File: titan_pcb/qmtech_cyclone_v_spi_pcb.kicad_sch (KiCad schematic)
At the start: 5 parts, among them J1 FPGA U8, J2 FPGA U7, J3 DUMMY_JTAG, U1 ESP32-DevKitC, U2 Teensy3.2

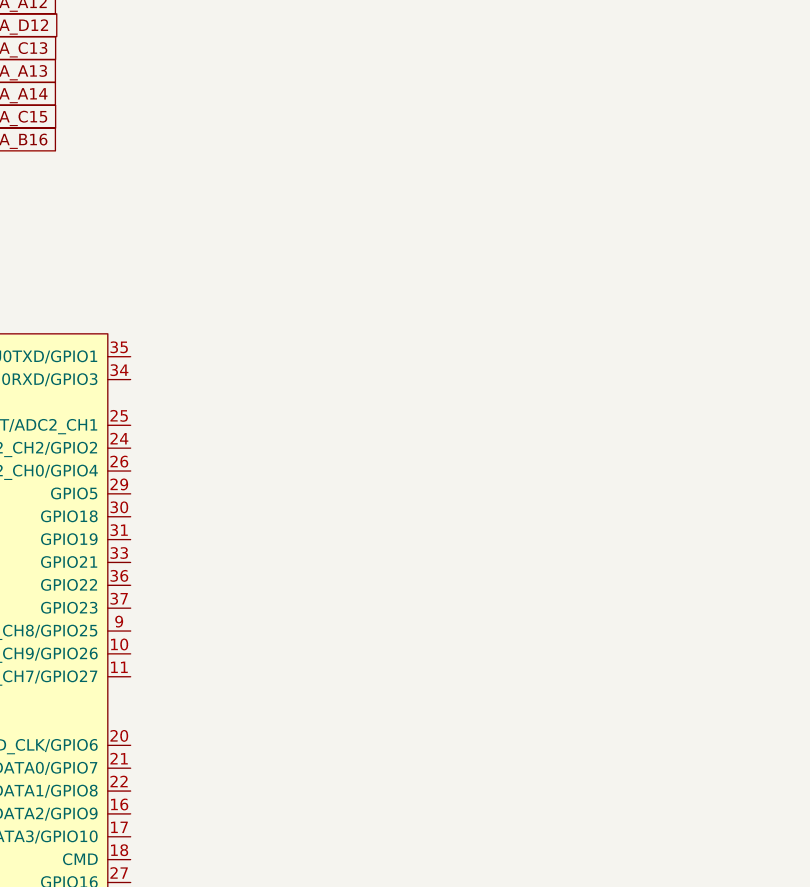
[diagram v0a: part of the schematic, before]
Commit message: added pico to pcb
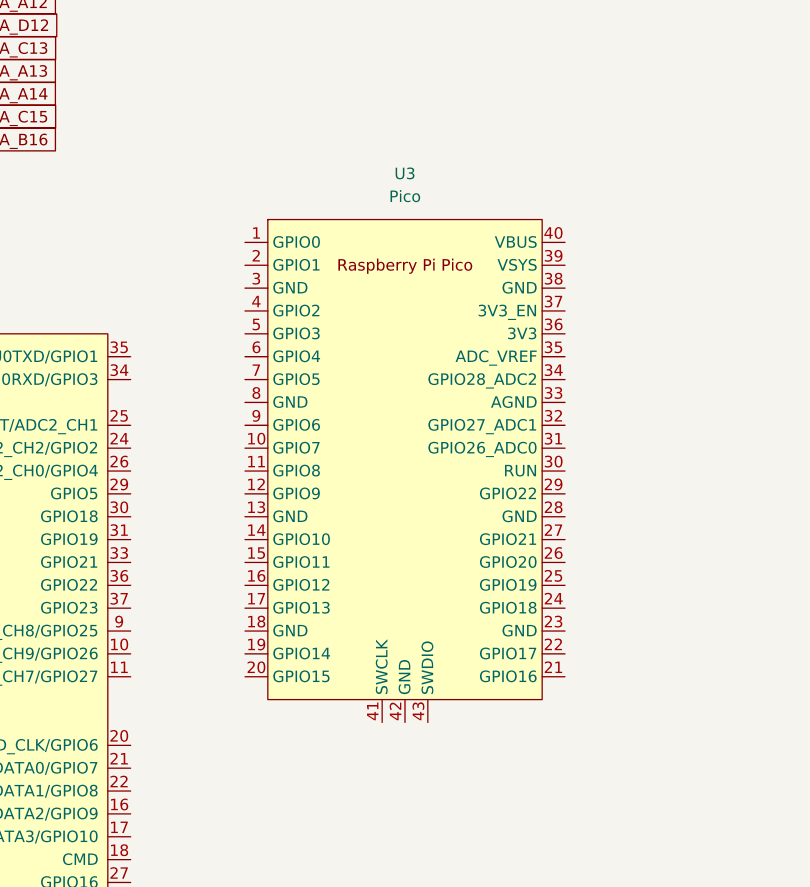
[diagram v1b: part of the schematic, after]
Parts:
- added U3: Pico, MCU_RaspberryPi_and_Boards:RPi_Pico_SMD_TH, symbol MCU_RaspberryPi_and_Boards:Pico
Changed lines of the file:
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@@
+    )
+  )
+  (symbol (lib_id "MCU_RaspberryPi_and_Boards:Pico") (at 176.53 133.35 0) (unit 1)
+    (in_bom yes) (on_board yes) (dnp no) (fields_autoplaced)
+    (property "Reference" "U3" (at 176.53 101.6 0)
+      (effects (font (size 1.27 1.27)))
+    )
+    (property "Value" "Pico" (at 176.53 104.14 0)
+      (effects (font (size 1.27 1.27)))
+    )
+    (property "Footprint" "MCU_RaspberryPi_and_Boards:RPi_Pico_SMD_TH" (at 176.53 133.35 90)
+      (effects (font (size 1.27 1.27)) hide)
+    )
+    (property "Datasheet" "" (at 176.53 133.35 0)
+      (effects (font (size 1.27 1.27)) hide)
+    )
+    (pin "1")
+    (pin "10")
+    (pin "11")
+    (pin "12")
+    (pin "13")
+    (pin "14")
+    (pin "15")
+    (pin "16")
+    (pin "17")
+    (pin "18")
+    (pin "19")
+    (pin "2")
+    (pin "20")
+    (pin "21")
+    (pin "22")
+    (pin "23")
+    (pin "24")
+    (pin "25")
+    (pin "26")
+    (pin "27")
+    (pin "28")
+    (pin "29")
+    (pin "3")
+    (pin "30")
+    (pin "31")
+    (pin "32")
+    (pin "33")
+    (pin "34")
+    (pin "35")
+    (pin "36")
+    (pin "37")
+    (pin "38")
+    (pin "39")
+    (pin "4")
+    (pin "40")
+    (pin "41")
+    (pin "42")
+    (pin "43")
+    (pin "5")
+    (pin "6")
+    (pin "7")
+    (pin "8")
+    (pin "9")
+    (instances
+      (project "qmtech_cyclone_v_spi_pcb"
+        (path "/6b222715-3ff4-46c6-84bf-6d2ef29db0c3"
+          (reference "U3") (unit 1)
+        )
+      )
     )
   )

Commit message: basic board layout with pin assignments between MCUs and FPGA
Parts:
- added Brd1: OLED, SSD1306:128x64OLED, symbol SSD1306-128x64_OLED:SSD1306
- added J15: teensy3.2_left_header_double, Connector_PinSocket_2.54mm:PinSocket_2x14_P2.54mm_Vertical, symbol Connector_Generic:Conn_02x14_Odd_Even
- added J16: pico_right_header_double, Connector_PinSocket_2.54mm:PinSocket_2x20_P2.54mm_Vertical, symbol Connector_Generic:Conn_02x20_Odd_Even
- added J4: esp_right_header_double, Connector_PinSocket_2.54mm:PinSocket_2x19_P2.54mm_Vertical, symbol Connector_Generic:Conn_02x19_Odd_Even
- added J5: pico_left_header_double, Connector_PinSocket_2.54mm:PinSocket_2x20_P2.54mm_Vertical, symbol Connector_Generic:Conn_02x20_Odd_Even
- added J7: esp_left_header_double, Connector_PinSocket_2.54mm:PinSocket_2x19_P2.54mm_Vertical, symbol Connector_Generic:Conn_02x19_Odd_Even
- added J8: teensy3.2_right_header_double, Connector_PinSocket_2.54mm:PinSocket_2x14_P2.54mm_Vertical, symbol Connector_Generic:Conn_02x14_Odd_Even
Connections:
- net BANK_5A_P16: now also J7.29 (Pin_29), J7.30 (Pin_30)
- net BANK_5A_P17: now also J7.25 (Pin_25), J7.26 (Pin_26)
- net BANK_5B_M18: now also J4.19 (Pin_19), J4.20 (Pin_20)
- net BANK_5B_M20: now also J4.15 (Pin_15), J4.16 (Pin_16)
- net BANK_5B_M21: now also J4.3 (Pin_3), J4.4 (Pin_4)
- net BANK_5B_N19: now also J4.17 (Pin_17), J4.18 (Pin_18)
- net BANK_5B_N20: now also J4.31 (Pin_31), J4.32 (Pin_32)
- net BANK_5B_N21: now also J7.23 (Pin_23), J7.24 (Pin_24)
- net BANK_7A_B15: now also J15.17 (Pin_17), J15.18 (Pin_18)
- net BANK_7A_B16: now also J8.25 (Pin_25), J8.26 (Pin_26)
- net BANK_7A_C13: now also J8.27 (Pin_27), J8.28 (Pin_28)
- net BANK_7A_C15: now also J15.19 (Pin_19), J15.20 (Pin_20)
- net BANK_7A_C16: now also J8.11 (Pin_11), J8.12 (Pin_12)
- net BANK_7A_D12: now also J15.27 (Pin_27), J15.28 (Pin_28)
- net BANK_7A_D13: now also J8.13 (Pin_13), J8.14 (Pin_14)
- net BANK_7A_E12: now also J15.25 (Pin_25), J15.26 (Pin_26)
- net BANK_8A_A5: now also J5.21 (Pin_21), J5.22 (Pin_22)
- net BANK_8A_B10: now also J5.10 (Pin_10), J5.9 (Pin_9)
- net BANK_8A_B5: now also J5.19 (Pin_19), J5.20 (Pin_20)
- net BANK_8A_B6: now also J5.23 (Pin_23), J5.24 (Pin_24)
- net BANK_8A_B7: now also J5.17 (Pin_17), J5.18 (Pin_18)
- net BANK_8A_C9: now also J5.11 (Pin_11), J5.12 (Pin_12)
- net BANK_8A_F10: now also J5.7 (Pin_7), J5.8 (Pin_8)
- net BANK_8A_G10: now also J5.13 (Pin_13), J5.14 (Pin_14)
- new net ESP_3V3: J7.1 (Pin_1), J7.2 (Pin_2)
- new net ESP_5V: J7.37 (Pin_37), J7.38 (Pin_38)
- new net ESP_EN_RST: J7.3 (Pin_3), J7.4 (Pin_4)
- new net ESP_GND: J4.1 (Pin_1), J4.13 (Pin_13), J4.14 (Pin_14), J4.2 (Pin_2), J7.27 (Pin_27), J7.28 (Pin_28)
- new net ESP_GPIO0: J4.27 (Pin_27), J4.28 (Pin_28)
- new net ESP_GPIO1: J4.7 (Pin_7), J4.8 (Pin_8)
- new net ESP_GPIO10_NC: J7.33 (Pin_33), J7.34 (Pin_34)
- new net ESP_GPIO11_NC: J7.35 (Pin_35), J7.36 (Pin_36)
- new net ESP_GPIO16: J4.23 (Pin_23), J4.24 (Pin_24)
- new net ESP_GPIO17: J4.21 (Pin_21), J4.22 (Pin_22)
- new net ESP_GPIO2: J4.29 (Pin_29), J4.30 (Pin_30)
- new net ESP_GPIO25: J7.17 (Pin_17), J7.18 (Pin_18)
- new net ESP_GPIO26: J7.19 (Pin_19), J7.20 (Pin_20)
- new net ESP_GPIO27: J7.21 (Pin_21), J7.22 (Pin_22)
- new net ESP_GPIO3: J4.10 (Pin_10), J4.9 (Pin_9)
- new net ESP_GPIO32: J7.13 (Pin_13), J7.14 (Pin_14)
- new net ESP_GPIO33: J7.15 (Pin_15), J7.16 (Pin_16)
- new net ESP_GPIO4: J4.25 (Pin_25), J4.26 (Pin_26)
- new net ESP_GPIO6_NC: J4.37 (Pin_37), J4.38 (Pin_38)
- new net ESP_GPIO7_NC: J4.35 (Pin_35), J4.36 (Pin_36)
- new net ESP_GPIO8_NC: J4.33 (Pin_33), J4.34 (Pin_34)
- new net ESP_GPIO9_NC: J7.31 (Pin_31), J7.32 (Pin_32)
- new net ESP_GPIX34: J7.10 (Pin_10), J7.9 (Pin_9)
- new net ESP_GPIX35: J7.11 (Pin_11), J7.12 (Pin_12)
- new net ESP_I2C_SCL_GPIO22: J4.5 (Pin_5), J4.6 (Pin_6)
- new net ESP_I2C_SDA_GPIO21: J4.11 (Pin_11), J4.12 (Pin_12)
- new net ESP_SVN_GPIX39: J7.7 (Pin_7), J7.8 (Pin_8)
- new net ESP_SVP_GPIX36: J7.5 (Pin_5), J7.6 (Pin_6)
- new net PICO_3V3: J16.10 (Pin_10), J16.9 (Pin_9)
- new net PICO_3V3_EN: J16.7 (Pin_7), J16.8 (Pin_8)
- new net PICO_ADC_REF: J16.11 (Pin_11), J16.12 (Pin_12)
- new net PICO_GND: J16.15 (Pin_15), J16.16 (Pin_16), J16.25 (Pin_25), J16.26 (Pin_26), J16.35 (Pin_35), J16.36 (Pin_36), J16.5 (Pin_5), J16.6 (Pin_6), J5.15 (Pin_15), J5.16 (Pin_16), J5.25 (Pin_25), J5.26 (Pin_26), J5.35 (Pin_35), J5.36 (Pin_36), J5.5 (Pin_5), J5.6 (Pin_6)
- new net PICO_GPIO28: J16.13 (Pin_13), J16.14 (Pin_14)
- new net PICO_GPIO_22: J16.23 (Pin_23), J16.24 (Pin_24)
- new net PICO_I2C0_SCL_GPIO21: J16.27 (Pin_27), J16.28 (Pin_28)
- new net PICO_I2C0_SDA_GPIO20: J16.29 (Pin_29), J16.30 (Pin_30)
- new net PICO_I2C1_SCL_GPIO27: J16.17 (Pin_17), J16.18 (Pin_18)
- new net PICO_I2C1_SDA_GPIO26: J16.19 (Pin_19), J16.20 (Pin_20)
- new net PICO_RUN: J16.21 (Pin_21), J16.22 (Pin_22)
- new net PICO_SPI0_CS_I2C0_SCL_GPIO1: J5.3 (Pin_3), J5.4 (Pin_4)
- new net PICO_SPI0_CS_I2C0_SCL_GPIO17: J16.37 (Pin_37), J16.38 (Pin_38)
- new net PICO_SPI0_DIN_I2C0_SDA_GPIO0: J5.1 (Pin_1), J5.2 (Pin_2)
- new net PICO_SPI0_DIN_I2C0_SDA_GPIO16: J16.39 (Pin_39), J16.40 (Pin_40)
- new net PICO_SPI0_DOUT_I2C1_SCL_GPIO19: J16.31 (Pin_31), J16.32 (Pin_32)
- new net PICO_SPI0_SCLK_I2C1_SDA_GPIO18: J16.33 (Pin_33), J16.34 (Pin_34)
- new net PICO_SPI1_CS_I2C0_SCL_GPIO13: J5.33 (Pin_33), J5.34 (Pin_34)
- new net PICO_SPI1_DIN_I2C0_SDA_GPIO12: J5.31 (Pin_31), J5.32 (Pin_32)
- new net PICO_SPI1_DOUT_I2C1_SCL_GPIO15: J5.39 (Pin_39), J5.40 (Pin_40)
- new net PICO_SPI1_DOUT_I2C_SCL_GPIO11: J5.29 (Pin_29), J5.30 (Pin_30)
- new net PICO_SPI1_SCLK_I2C1_SDA_GPIO10: J5.27 (Pin_27), J5.28 (Pin_28)
- new net PICO_SPI1_SCLK_I2C1_SDA_GPIO14: J5.37 (Pin_37), J5.38 (Pin_38)
- new net PICO_VBUS: J16.1 (Pin_1), J16.2 (Pin_2)
- new net PICO_VSYS: J16.3 (Pin_3), J16.4 (Pin_4)
- new net TEENSY_3V3: J8.5 (Pin_5), J8.6 (Pin_6)
- new net TEENSY_AGND: J8.3 (Pin_3), J8.4 (Pin_4)
- new net TEENSY_GND: J15.1 (Pin_1), J15.2 (Pin_2)
- new net TEENSY_GPIO_0: J15.3 (Pin_3), J15.4 (Pin_4)
- new net TEENSY_GPIO_1: J15.5 (Pin_5), J15.6 (Pin_6)
- new net TEENSY_GPIO_16: J8.21 (Pin_21), J8.22 (Pin_22)
- new net TEENSY_GPIO_17: J8.19 (Pin_19), J8.20 (Pin_20)
- new net TEENSY_GPIO_18: J8.17 (Pin_17), J8.18 (Pin_18)
- new net TEENSY_GPIO_19: J8.15 (Pin_15), J8.16 (Pin_16)
- new net TEENSY_GPIO_2: J15.7 (Pin_7), J15.8 (Pin_8)
- new net TEENSY_GPIO_22: J8.10 (Pin_10), J8.9 (Pin_9)
- new net TEENSY_GPIO_23: J8.7 (Pin_7), J8.8 (Pin_8)
- new net TEENSY_GPIO_3: J15.10 (Pin_10), J15.9 (Pin_9)
- new net TEENSY_GPIO_4: J15.11 (Pin_11), J15.12 (Pin_12)
- new net TEENSY_GPIO_5: J15.13 (Pin_13), J15.14 (Pin_14)
- new net TEENSY_SPI_CS_0: J15.23 (Pin_23), J15.24 (Pin_24)
- new net TEENSY_SPI_CS_1: J15.21 (Pin_21), J15.22 (Pin_22)
- new net TEENSY_SPI_CS_2: J8.23 (Pin_23), J8.24 (Pin_24)
- new net TEENSY_VIN: J8.1 (Pin_1), J8.2 (Pin_2)
- new net TEESNY_GPIO_6: J15.15 (Pin_15), J15.16 (Pin_16)
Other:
- moved on the sheet: J1, J2, J3, U1, U2, U3

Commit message: finalised pcb - pinouts checked, silkscreen  and ground plane added
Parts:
- removed Brd1: OLED, SSD1306:128x64OLED, symbol SSD1306-128x64_OLED:SSD1306
- added H1, H2, H3, H4, H5, H6, H7, H8: MountingHole, MountingHole:MountingHole_2.2mm_M2_ISO7380_Pad_TopBottom, symbol Mechanical:MountingHole
- added J10: OLED_CONN_0, Connector_PinSocket_2.54mm:PinSocket_1x04_P2.54mm_Vertical, symbol Connector_Generic:Conn_01x04
- added J11: OLED_CONN_1, Connector_PinSocket_2.54mm:PinSocket_1x04_P2.54mm_Vertical, symbol Connector_Generic:Conn_01x04
- added J12: CH341_PRG_CONN, Connector_PinSocket_2.54mm:PinSocket_2x08_P2.54mm_Vertical, symbol Connector_Generic:Conn_02x08_Odd_Even
- added J13: SPI_HEADER_0, Connector_PinHeader_2.54mm:PinHeader_1x05_P2.54mm_Vertical, symbol Connector_Generic:Conn_01x05
- added J14: SPI_HEADER_1, Connector_PinHeader_2.54mm:PinHeader_1x05_P2.54mm_Vertical, symbol Connector_Generic:Conn_01x05
- added J15: PICO_I2C0_PULLUPS, Connector_PinHeader_2.54mm:PinHeader_2x02_P2.54mm_Vertical, symbol Connector_Generic:Conn_02x02_Odd_Even
- added J16: PICO_I2C1_PULLUPS, Connector_PinHeader_2.54mm:PinHeader_2x02_P2.54mm_Vertical, symbol Connector_Generic:Conn_02x02_Odd_Even
- added J17: TEENSY_I2C_PULLUPS, Connector_PinHeader_2.54mm:PinHeader_2x02_P2.54mm_Vertical, symbol Connector_Generic:Conn_02x02_Odd_Even
- added J18: ESP32_I2C_PULLUPS, Connector_PinHeader_2.54mm:PinHeader_2x02_P2.54mm_Vertical, symbol Connector_Generic:Conn_02x02_Odd_Even
- added J9: OLED_JMP, Connector_PinHeader_2.54mm:PinHeader_2x06_P2.54mm_Vertical, symbol Connector_Generic:Conn_02x06_Odd_Even
- added R1, R2, R3, R4, R5, R6, R7, R8: 2K, Resistor_SMD:R_1206_3216Metric_Pad1.30x1.75mm_HandSolder, symbol Device:R
- J3: renamed from J15; value teensy3.2_left_header_double -> T3.2_LEFT_HEADER
- J4: renamed from J8; value teensy3.2_right_header_double -> T3.2_RIGHT_HEADER
- J5: renamed from J4; value esp_right_header_double -> ESP_LEFT_HEADER
- J6: renamed from J7; value esp_left_header_double -> ESP_RIGHT_HEADER
- J7: renamed from J5; value pico_left_header_double -> PICO_LEFT_HEADER
- J8: renamed from J16; value pico_right_header_double -> PICO_RIGHT_HEADER
- renumbered J2 to J1, J1 to J2, J3 to Jx1
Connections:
- net ESP_GND is gone; now on net GND: J5.1 (Pin_1), J5.13 (Pin_13), J5.14 (Pin_14), J5.2 (Pin_2), J6.27 (Pin_27), J6.28 (Pin_28)
- net PICO_GND is gone; now on net GND: J7.15 (Pin_15), J7.16 (Pin_16), J7.25 (Pin_25), J7.26 (Pin_26), J7.35 (Pin_35), J7.36 (Pin_36), J7.5 (Pin_5), J7.6 (Pin_6), J8.15 (Pin_15), J8.16 (Pin_16), J8.25 (Pin_25), J8.26 (Pin_26), J8.35 (Pin_35), J8.36 (Pin_36), J8.5 (Pin_5), J8.6 (Pin_6)
- net PICO_SPI1_CS_I2C0_SCL_GPIO13 is gone; now on net BANK_8A_C6: J7.33 (Pin_33), J7.34 (Pin_34)
- net PICO_SPI1_DIN_I2C0_SDA_GPIO12 is gone; now on net BANK_8A_D9: J7.31 (Pin_31), J7.32 (Pin_32)
- net PICO_SPI1_DOUT_I2C_SCL_GPIO11 is gone; now on net BANK_8A_A5: J7.29 (Pin_29), J7.30 (Pin_30)
- net PICO_SPI1_SCLK_I2C1_SDA_GPIO10 is gone; now on net BANK_8A_B7: J7.27 (Pin_27), J7.28 (Pin_28)
- net TEENSY_GND is gone; now on net GND: J3.1 (Pin_1), J3.2 (Pin_2)
- net 3V3: now also J10.2 (Pin_2), J11.2 (Pin_2)
- net BANK_2A_U1: now also J13.2 (Pin_2)
- net BANK_2A_U2: now also J13.3 (Pin_3)
- net BANK_2A_W2: now also J13.5 (Pin_5)
- net BANK_2A_Y3: now also J13.4 (Pin_4)
- net BANK_4A_AA15: now also J14.2 (Pin_2)
- net BANK_4A_AB15: now also J14.3 (Pin_3)
- net BANK_4A_Y14: now also J14.5 (Pin_5)
- net BANK_4A_Y15: now also J14.4 (Pin_4)
- net BANK_5A_P16: no longer J6.29 (Pin_29), J6.30 (Pin_30)
- net BANK_5A_P17: now also J6.23 (Pin_23), J6.24 (Pin_24); no longer J6.25 (Pin_25), J6.26 (Pin_26)
- net BANK_5A_R21: now also J6.29 (Pin_29), J6.30 (Pin_30)
- net BANK_5A_T19: now also J6.25 (Pin_25), J6.26 (Pin_26)
- net BANK_5B_K17: now also J12.13 (Pin_13)
- net BANK_5B_K21: now also J12.9 (Pin_9)
- net BANK_5B_K22: now also J12.11 (Pin_11)
- net BANK_5B_L17: now also J12.15 (Pin_15)
- net BANK_5B_L19: now also J5.15 (Pin_15), J5.16 (Pin_16)
- net BANK_5B_L22: now also J5.3 (Pin_3), J5.4 (Pin_4)
- net BANK_5B_M16: now also J12.7 (Pin_7)
- net BANK_5B_M18: no longer J5.19 (Pin_19), J5.20 (Pin_20)
- net BANK_5B_M20: now also J5.19 (Pin_19), J5.20 (Pin_20); no longer J5.15 (Pin_15), J5.16 (Pin_16)
- net BANK_5B_M21: no longer J5.3 (Pin_3), J5.4 (Pin_4)
- net BANK_5B_N16: now also J12.5 (Pin_5)
- net BANK_5B_N20: no longer J5.31 (Pin_31), J5.32 (Pin_32)
- net BANK_5B_N21: now also J5.31 (Pin_31), J5.32 (Pin_32); no longer J6.23 (Pin_23), J6.24 (Pin_24)
- net BANK_7A_A15: now also J4.25 (Pin_25), J4.26 (Pin_26)
- net BANK_7A_B12: now also J3.25 (Pin_25), J3.26 (Pin_26)
- net BANK_7A_B13: now also J3.17 (Pin_17), J3.18 (Pin_18)
- net BANK_7A_B15: now also J4.13 (Pin_13), J4.14 (Pin_14); no longer J3.17 (Pin_17), J3.18 (Pin_18)
- net BANK_7A_B16: no longer J4.25 (Pin_25), J4.26 (Pin_26)
- net BANK_7A_C11: now also J3.27 (Pin_27), J3.28 (Pin_28)
- net BANK_7A_C13: no longer J4.27 (Pin_27), J4.28 (Pin_28)
- net BANK_7A_C15: no longer J3.19 (Pin_19), J3.20 (Pin_20)
- net BANK_7A_D12: no longer J3.27 (Pin_27), J3.28 (Pin_28)
- net BANK_7A_D13: now also J3.19 (Pin_19), J3.20 (Pin_20); no longer J4.13 (Pin_13), J4.14 (Pin_14)
- net BANK_7A_E12: now also J4.27 (Pin_27), J4.28 (Pin_28); no longer J3.25 (Pin_25), J3.26 (Pin_26)
- net BANK_8A_A10: now also J7.11 (Pin_11), J7.12 (Pin_12)
- net BANK_8A_A5: no longer J7.21 (Pin_21), J7.22 (Pin_22)
- net BANK_8A_A8: now also J7.13 (Pin_13), J7.14 (Pin_14)
- net BANK_8A_B10: no longer J7.10 (Pin_10), J7.9 (Pin_9)
- net BANK_8A_B5: no longer J7.19 (Pin_19), J7.20 (Pin_20)
- net BANK_8A_B6: no longer J7.23 (Pin_23), J7.24 (Pin_24)
- net BANK_8A_B7: no longer J7.17 (Pin_17), J7.18 (Pin_18)
- net BANK_8A_C9: now also J7.10 (Pin_10), J7.9 (Pin_9); no longer J7.11 (Pin_11), J7.12 (Pin_12)
- net BANK_8A_G10: no longer J7.13 (Pin_13), J7.14 (Pin_14)
- net ESP_3V3: now also R7.2, R8.2
- net ESP_I2C_SCL_GPIO22: now also J18.1 (Pin_1), J9.10 (Pin_10)
- net ESP_I2C_SDA_GPIO21: now also J18.2 (Pin_2), J9.12 (Pin_12)
- net GND: now also J10.1 (Pin_1), J11.1 (Pin_1), J12.16 (Pin_16), J12.3 (Pin_3), J12.8 (Pin_8), J13.1 (Pin_1), J14.1 (Pin_1)
- net PICO_3V3: now also R1.2, R2.2, R3.2, R4.2
- net PICO_SPI0_CS_I2C0_SCL_GPIO17: now also J15.1 (Pin_1)
- net PICO_SPI0_DIN_I2C0_SDA_GPIO16: now also J15.2 (Pin_2)
- net PICO_SPI1_DOUT_I2C1_SCL_GPIO15: now also J16.2 (Pin_2), J9.2 (Pin_2)
- net PICO_SPI1_SCLK_I2C1_SDA_GPIO14: now also J16.1 (Pin_1), J9.4 (Pin_4)
- net TEENSY_3V3: now also R5.2, R6.2
- net TEENSY_GPIO_18 renamed TEENSY_GPIO_18_SDA
- net TEENSY_GPIO_18_SDA: now also J17.2 (Pin_2), J9.8 (Pin_8)
- net TEENSY_GPIO_19 renamed TEENSY_GPIO_19_SCL
- net TEENSY_GPIO_19_SCL: now also J17.1 (Pin_1), J9.6 (Pin_6)
- new net: J15.4 (Pin_4), R1.1
- new net: J17.3 (Pin_3), R6.1
- new net: J17.4 (Pin_4), R5.1
- new net: J16.4 (Pin_4), R3.1
- new net: J18.3 (Pin_3), R8.1
- new net: J16.3 (Pin_3), R4.1
- new net: J15.3 (Pin_3), R2.1
- new net: J18.4 (Pin_4), R7.1
- new net OLED_SCL: J10.3 (Pin_3), J11.3 (Pin_3), J9.1 (Pin_1), J9.5 (Pin_5), J9.9 (Pin_9)
- new net OLED_SDA: J10.4 (Pin_4), J11.4 (Pin_4), J9.11 (Pin_11), J9.3 (Pin_3), J9.7 (Pin_7)
- new net PICO_SPI0_DOUT_I2C1_SCL_GPIO7: J7.19 (Pin_19), J7.20 (Pin_20)
- new net PICO_SPI0_SCLK_I2C1_SDA_GPIO6: J7.17 (Pin_17), J7.18 (Pin_18)
- new net PICO_SPI1_CS_I2C0_SCL_GPIO9: J7.23 (Pin_23), J7.24 (Pin_24)
- new net PICO_SPI1_DIN_I2C0_SDA_GPIO8: J7.21 (Pin_21), J7.22 (Pin_22)
- new net PRG_RXD: J12.14 (Pin_14)
- new net PRG_SCL: J12.6 (Pin_6)
- new net PRG_SDA: J12.4 (Pin_4)
- new net PRG_TXD: J12.12 (Pin_12)
- new net PRG_VCC: J12.1 (Pin_1), J12.10 (Pin_10), J12.2 (Pin_2)
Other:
- note added: "AUX. FPGA-SPI HEADERS"
- note added: "CH341 SPI-USB"
- note added: "ESP32"
- note added: "OLED + I2C SELECTOR"
- note added: "PICO"
- note added: "TEENSY 3.2"
- moved on the sheet: J1, J2, J3, J4, J5, J6, J7, J8, Jx1, U1, U2, U3

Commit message: (wip) 3v3 supply
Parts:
- added C1, C2: 10uF, Capacitor_Tantalum_SMD:CP_EIA-3216-18_Kemet-A_Pad1.58x1.35mm_HandSolder, symbol Device:C_Polarized
- added J19: Barrel_Jack_MountingPin, Connector_BarrelJack:BarrelJack_CUI_PJ-063AH_Horizontal, symbol Connector:Barrel_Jack_MountingPin
- added J20, J21, J22: Conn_01x02, Connector_PinHeader_2.54mm:PinHeader_1x02_P2.54mm_Vertical, symbol Connector_Generic:Conn_01x02
- added SW1: SW_SPDT, symbol Switch:SW_SPDT
- added U1: LM1084-3.3, Package_TO_SOT_SMD:TO-263-3_TabPin2, symbol Regulator_Linear:LM1084-3.3
- renumbered U1 to Ux1, U2 to Ux2, U3 to Ux3
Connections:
- net 3V3: now also C2.1, J20.1 (Pin_1), J21.1 (Pin_1), J22.1 (Pin_1), SW1.2 (B), U1.2 (VO); no longer J1.3 (Pin_3), J1.4 (Pin_4), J2.3 (Pin_3), J2.4 (Pin_4)
- net BANK_2A_AA1: now also J14.3 (Pin_3)
- net BANK_2A_AA2: now also J14.2 (Pin_2)
- net BANK_2A_N1: now also J13.4 (Pin_4)
- net BANK_2A_N2: now also J13.5 (Pin_5)
- net BANK_2A_W2: now also J14.5 (Pin_5); no longer J13.5 (Pin_5)
- net BANK_2A_Y3: now also J14.4 (Pin_4); no longer J13.4 (Pin_4)
- net BANK_4A_AA15: no longer J14.2 (Pin_2)
- net BANK_4A_AB15: no longer J14.3 (Pin_3)
- net BANK_4A_Y14: no longer J14.5 (Pin_5)
- net BANK_4A_Y15: no longer J14.4 (Pin_4)
- net ESP_3V3: now also J22.2 (Pin_2), SW1.1 (A)
- net GND: now also C1.2, C2.2, J19.2, J19.MP (MountPin), U1.1 (GND)
- net PICO_3V3: now also J20.2 (Pin_2)
- net TEENSY_3V3: now also J21.2 (Pin_2)
- new net: C1.1, J19.1, U1.3 (VI)
- new net FPGA_3V3: J1.3 (Pin_3), J1.4 (Pin_4), J2.3 (Pin_3), J2.4 (Pin_4)

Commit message: updated silkscreen, added diode for pico power supply, consolidated part value fields for BOM
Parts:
- removed SW1: SW_SPDT, symbol Switch:SW_SPDT
- added D1: 1N4148, Diode_THT:D_DO-35_SOD27_P7.62mm_Horizontal, symbol Diode:1N4148
- added J23: PWR_SW, Connector_PinHeader_2.54mm:PinHeader_1x02_P2.54mm_Vertical, symbol Connector_Generic:Conn_01x02
- J1: value FPGA U7 -> FPGA; SIDE (none) -> U7
- J10: value OLED_CONN_0 -> OLED_CONN; Number (none) -> 0
- J11: value OLED_CONN_1 -> OLED_CONN; Number (none) -> 1
- J13: value SPI_HEADER_0 -> SPI_HEADER; Number (none) -> 0
- J14: value SPI_HEADER_1 -> SPI_HEADER; Number (none) -> 1
- J15: value PICO_I2C0_PULLUPS -> I2C_PULLUP; Target (none) -> PICO_I2C_0
- J16: value PICO_I2C1_PULLUPS -> I2C_PULLUP; Target (none) -> PICO_I2C_1
- J17: value TEENSY_I2C_PULLUPS -> I2C_PULLUP; Target (none) -> TEENSY
- J18: value ESP32_I2C_PULLUPS -> I2C_PULLUP; Target (none) -> ESP32
- J2: value FPGA U8 -> FPGA; Side (none) -> U8
- J20: value Conn_01x02 -> PWR_SW; Target (none) -> PICO
- J21: value Conn_01x02 -> PWR_SW; Target (none) -> TEENSY
- J22: value Conn_01x02 -> PWR_SW; Target (none) -> ESP32
- J3: value T3.2_LEFT_HEADER -> TEENSY; Side (none) -> LEFT
- J4: value T3.2_RIGHT_HEADER -> TEENSY; Side (none) -> RIGHT
- J5: value ESP_LEFT_HEADER -> ESP; Side (none) -> LEFT
- J6: value ESP_RIGHT_HEADER -> ESP; Side (none) -> RIGHT
- J7: value PICO_LEFT_HEADER -> PICO; Side (none) -> LEFT
- J8: value PICO_RIGHT_HEADER -> PICO; Side (none) -> RIGHT
- JX1: renamed from Jx1; now left out of the parts list
- UX1: renamed from Ux1; now left out of the parts list
- UX2: renamed from Ux2; now left out of the parts list
- UX3: renamed from Ux3; now left out of the parts list
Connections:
- net 3V3: now also R1.2, R2.2, R3.2, R4.2, R5.2, R6.2, R7.2, R8.2, J23.1 (Pin_1)
- net ESP_3V3: no longer R7.2, R8.2
- net PICO_3V3: no longer J20.2 (Pin_2), R1.2, R2.2, R3.2, R4.2
- net PICO_SPI0_CS_I2C0_SCL_GPIO17: no longer J15.1 (Pin_1)
- net PICO_SPI0_DIN_I2C0_SDA_GPIO16: no longer J15.2 (Pin_2)
- net PICO_SPI1_CS_I2C0_SCL_GPIO9: now also J15.1 (Pin_1)
- net PICO_SPI1_DIN_I2C0_SDA_GPIO8: now also J15.2 (Pin_2)
- net PICO_VSYS: now also D1.1 (K)
- net TEENSY_3V3: no longer R5.2, R6.2
- net VIN renamed FPGA_VIN
- net FPGA_VIN: now also J23.2 (Pin_2)
- new net: D1.2 (A), J20.2 (Pin_2)
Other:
- note added: "POWER SUPPLY + SWITCHES"
- note added: "TODO: ADD DIODE https://peppe8o.com/powering-the-raspberry-pi-pico-from-external-batteries/ https://www.reddit.com/r/raspberrypipico/comments/op74gm/question_about_powering_pi_pico/ https://www.reddit.com/r/raspberrypipico/comments/nu8u9l/powering_pico/"
- moved on the sheet: C1, C2, J1, J15, J19, J2, R1, R2, U1
